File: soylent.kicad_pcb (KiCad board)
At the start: 2 copper layers, 23 parts, among them J1 DB9_Female, J2 Conn_01x04, J3 Conn_01x04, J4 Conn_02x03_Counter_Clockwise, Q1 BC847BPN, Q2 BC847BPN, U1 ATtiny202-SS, U2 MIC5504-3.3YM5

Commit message: Drop a via
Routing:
- net VDD: track 44.2 -> 46.4 mm
- net GND: vias 4 -> 3
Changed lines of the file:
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@@
   (segment (start 228.0258 37.3126) (end 226.1108 39.2276) (width 0.25) (layer B.Cu) (net 1))
   (segment (start 234.5944 37.3126) (end 228.0258 37.3126) (width 0.25) (layer B.Cu) (net 1))
-  (via (at 241.6048 32.3826) (size 0.8) (drill 0.4) (layers F.Cu B.Cu) (net 1))
   (via (at 237.3884 29.9212) (size 0.8) (drill 0.4) (layers F.Cu B.Cu) (net 1))
   (segment (start 232.961611 56.076011) (end 225.0058 48.1202) (width 0.25) (layer F.Cu) (net 2))
@@
   (segment (start 248.3642 31.2626) (end 248.5992 31.0276) (width 0.25) (layer F.Cu) (net 3))
   (segment (start 239.8672 31.2626) (end 248.3642 31.2626) (width 0.25) (layer F.Cu) (net 3))
-  (segment (start 248.5992 32.655) (end 248.5992 31.0276) (width 0.25) (layer F.Cu) (net 3))
-  (segment (start 243.9416 37.3126) (end 248.5992 32.655) (width 0.25) (layer F.Cu) (net 3))
+  (segment (start 251.2236 39.2076) (end 252.3236 39.2076) (width 0.25) (layer F.Cu) (net 3))
+  (segment (start 248.5992 36.5832) (end 251.2236 39.2076) (width 0.25) (layer F.Cu) (net 3))
+  (segment (start 248.5992 31.0276) (end 248.5992 36.5832) (width 0.25) (layer F.Cu) (net 3))
   (segment (start 227.2058 49.539602) (end 227.2058 45.212) (width 0.25) (layer F.Cu) (net 4))
   (segment (start 235.798601 55.620988) (end 234.345799 55.620988) (width 0.25) (layer F.Cu) (net 4))

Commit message: Add edge cuts
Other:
- board outline added: 34.5 x 44.2 mm
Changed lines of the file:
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@@
   (general
     (thickness 1.6)
-    (drawings 2)
+    (drawings 6)
     (tracks 160)
     (zones 0)
@@
     )
   )
+  (gr_line (start 221.8944 64.008) (end 221.8944 19.7612) (layer Edge.Cuts) (width 0.1))
+  (gr_line (start 256.3876 64.008) (end 221.8944 64.008) (layer Edge.Cuts) (width 0.1))
+  (gr_line (start 256.3876 19.7612) (end 256.3876 64.008) (layer Edge.Cuts) (width 0.1))
+  (gr_line (start 221.8944 19.7612) (end 256.3876 19.7612) (layer Edge.Cuts) (width 0.1))
   (gr_text Vdd (at 254.6096 39.1668 90) (layer F.SilkS)
     (effects (font (size 1 1) (thickness 0.25)))

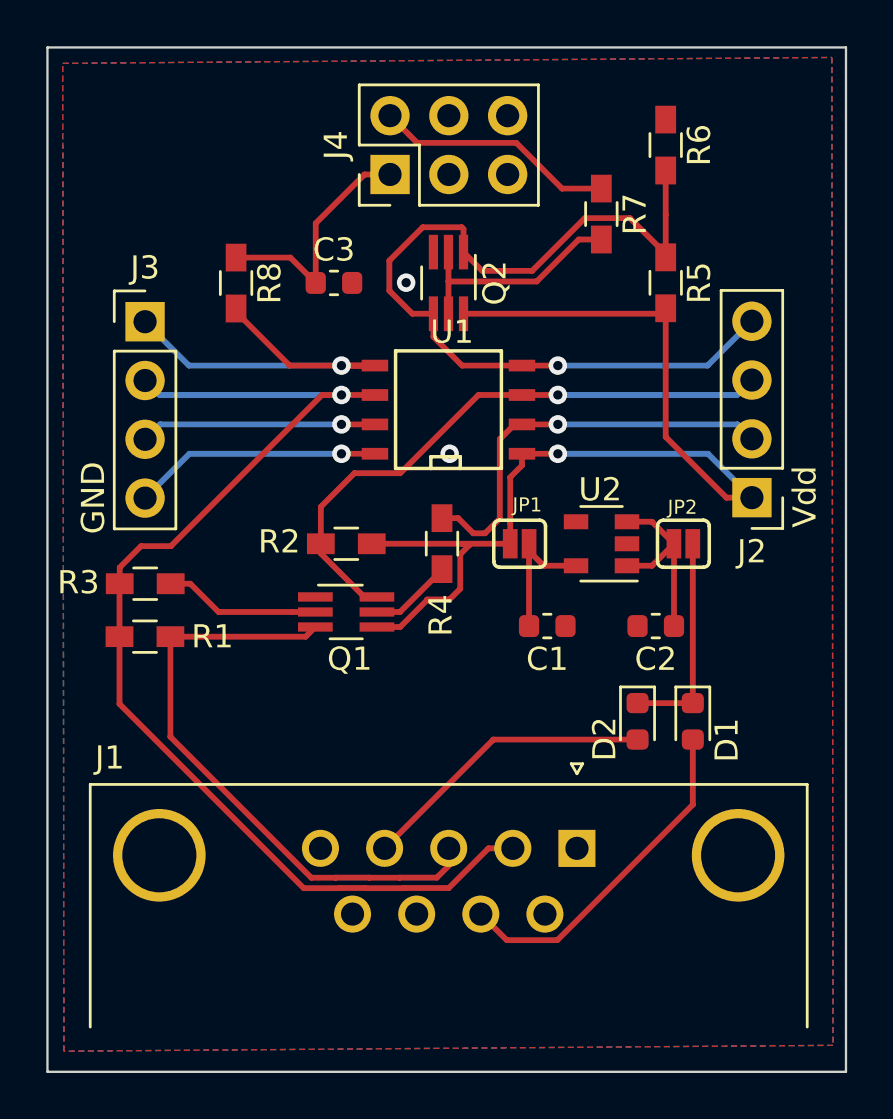
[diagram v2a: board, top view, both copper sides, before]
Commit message: Shrink cuts and zones
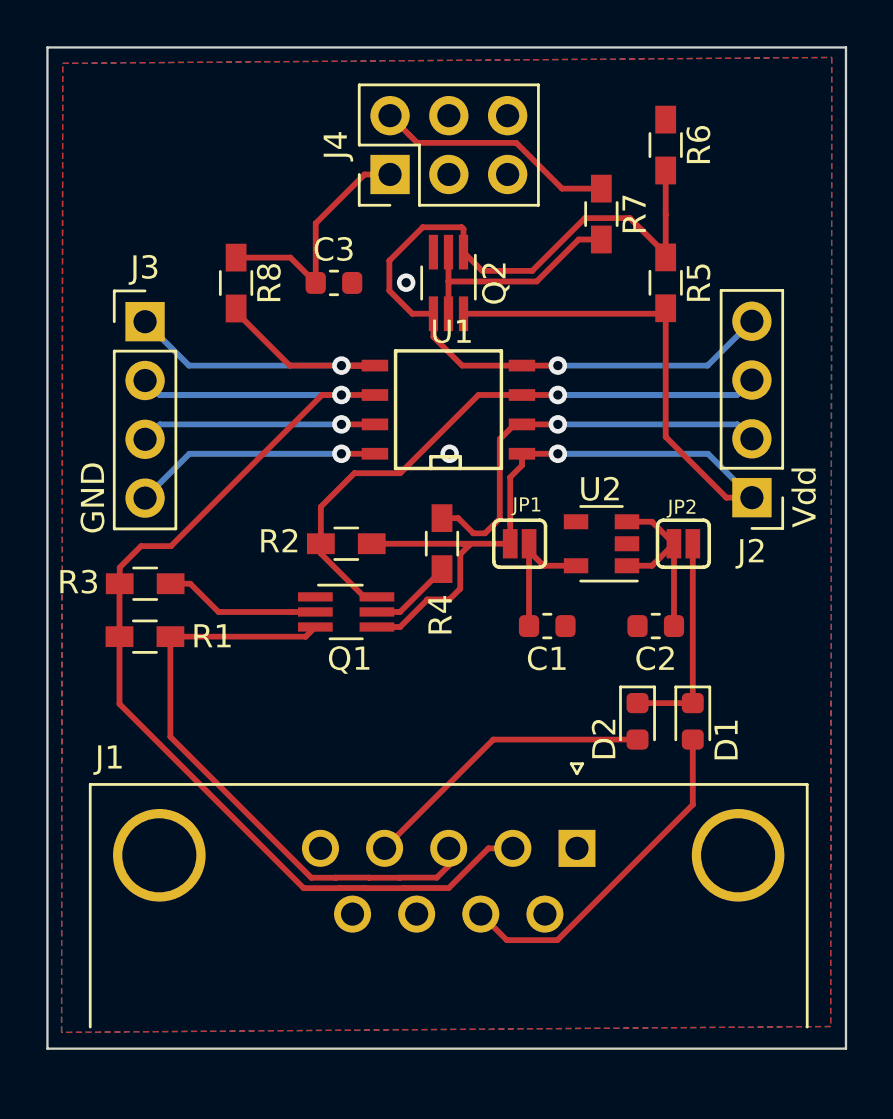
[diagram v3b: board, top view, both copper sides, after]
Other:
- board size 34.5 x 44.2 mm -> 34.5 x 43.2 mm
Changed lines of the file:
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@@
     )
   )
-  (gr_line (start 221.8944 64.008) (end 221.8944 19.7612) (layer Edge.Cuts) (width 0.1))
-  (gr_line (start 256.3876 64.008) (end 221.8944 64.008) (layer Edge.Cuts) (width 0.1))
-  (gr_line (start 256.3876 19.7612) (end 256.3876 64.008) (layer Edge.Cuts) (width 0.1))
+  (gr_line (start 221.8944 63.008) (end 221.8944 19.7612) (layer Edge.Cuts) (width 0.1))
+  (gr_line (start 256.3876 63.008) (end 221.8944 63.008) (layer Edge.Cuts) (width 0.1))
+  (gr_line (start 256.3876 19.7612) (end 256.3876 63.008) (layer Edge.Cuts) (width 0.1))
   (gr_line (start 221.8944 19.7612) (end 256.3876 19.7612) (layer Edge.Cuts) (width 0.1))
   (gr_text Vdd (at 254.6096 39.1668 90) (layer F.SilkS)
@@
     (polygon
       (pts
-        (xy 222.5548 20.447) (xy 255.778 20.193) (xy 255.8288 62.865) (xy 222.6056 63.119)
+        (xy 222.5548 20.447) (xy 255.778 20.193) (xy 255.7272 62.0522) (xy 222.504 62.3062)
       )
     )
@@
     (polygon
       (pts
-        (xy 222.5548 20.447) (xy 255.778 20.193) (xy 255.8288 62.865) (xy 222.6056 63.119)
+        (xy 222.5548 20.447) (xy 255.778 20.193) (xy 255.7272 62.0522) (xy 222.504 62.3062)
       )
     )

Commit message: Routing tweaks
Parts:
- moved C3 6.92 mm to (230.0, 24.5), turned to 90 degrees
- moved R6 0.17 mm to (248.6, 24.1)
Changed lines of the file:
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@@
     (thickness 1.6)
     (drawings 6)
-    (tracks 160)
+    (tracks 158)
     (zones 0)
     (modules 23)
@@
   )
   (module Capacitor_SMD:C_0603_1608Metric (layer F.Cu)
-    (at 234.2708 29.9326)
+    (at 230.0422 24.4601 90)
     (descr "Capacitor SMD 0603 (1608 Metric), square (rectangular) end terminal, IPC_7351 nominal, (Body size source: http://www.tortai-tech.com/upload/download/2011102023233369053.pdf), generated with kicad-footprint-generator")
     (tags capacitor)
     (attr smd)
-    (fp_text reference C3 (at 0 -1.43) (layer F.SilkS)
-      (effects (font (size 1 1) (thickness 0.15)))
-    )
-    (fp_text value .1u (at 0 1.43) (layer F.Fab)
-      (effects (font (size 1 1) (thickness 0.15)))
-    )
-    (fp_text user %R (at 0 0) (layer F.Fab)
+    (fp_text reference C3 (at 0 -1.43 90) (layer F.SilkS)
+      (effects (font (size 1 1) (thickness 0.15)))
+    )
+    (fp_text value .1u (at 0 1.43 90) (layer F.Fab)
+      (effects (font (size 1 1) (thickness 0.15)))
+    )
+    (fp_text user %R (at 0 0 90) (layer F.Fab)
       (effects (font (size 0.4 0.4) (thickness 0.06)))
     )
@@
     (fp_line (start -0.8 -0.4) (end 0.8 -0.4) (layer F.Fab) (width 0.1))
     (fp_line (start -0.8 0.4) (end -0.8 -0.4) (layer F.Fab) (width 0.1))
-    (pad 2 smd roundrect (at 0.7875 0) (size 0.875 0.95) (layers F.Cu F.Paste F.Mask) (roundrect_rratio 0.25)
+    (pad 2 smd roundrect (at 0.7875 0 90) (size 0.875 0.95) (layers F.Cu F.Paste F.Mask) (roundrect_rratio 0.25)
       (net 1 GND))
-    (pad 1 smd roundrect (at -0.7875 0) (size 0.875 0.95) (layers F.Cu F.Paste F.Mask) (roundrect_rratio 0.25)
+    (pad 1 smd roundrect (at -0.7875 0 90) (size 0.875 0.95) (layers F.Cu F.Paste F.Mask) (roundrect_rratio 0.25)
       (net 19 "Net-(C3-Pad1)"))
     (model ${KISYS3DMOD}/Capacitor_SMD.3dshapes/C_0603_1608Metric.wrl
@@
   )
   (module Resistors_SMD:R_0603_HandSoldering (layer F.Cu)
-    (at 248.5992 23.9776 270)
+    (at 248.5992 24.1476 270)
     (descr "Resistor SMD 0603, hand soldering")
     (tags "resistor 0603")
@@
     (tags "resistor 0603")
     (attr smd)
-    (fp_text reference R3 (at -2.884 -0.0508) (layer F.SilkS)
-      (effects (font (size 1 1) (thickness 0.15)))
-    )
-    (fp_text value 10k (at 3.3136 0) (layer F.Fab)
+    (fp_text reference R3 (at 3.043 0) (layer F.SilkS)
+      (effects (font (size 1 1) (thickness 0.15)))
+    )
+    (fp_text value 10k (at 0.0458 1.016) (layer F.Fab)
       (effects (font (size 1 1) (thickness 0.15)))
     )
@@
       (effects (font (size 1 1) (thickness 0.15)))
     )
-    (fp_text value 4k7 (at 3.382 0.0508) (layer F.Fab)
+    (fp_text value 4k7 (at 0.0458 -1.524) (layer F.Fab)
       (effects (font (size 1 1) (thickness 0.15)))
     )
@@
     )
   )
-  (module Pin_Headers:Pin_Header_Straight_2x03_Pitch2.54mm locked (layer F.Cu)
+  (module Pin_Headers:Pin_Header_Straight_2x03_Pitch2.54mm (layer F.Cu)
     (at 236.6922 25.2476 90)
     (descr "Through hole straight pin header, 2x03, 2.54mm pitch, double rows")
@@
   (segment (start 226.7558 36.0426) (end 226.1108 36.6876) (width 0.25) (layer B.Cu) (net 17))
   (segment (start 234.5944 36.0426) (end 226.7558 36.0426) (width 0.25) (layer B.Cu) (net 17))
-  (segment (start 248.5992 26.9908) (end 248.5992 28.8276) (width 0.25) (layer F.Cu) (net 15))
-  (segment (start 248.5992 25.0776) (end 248.5992 26.9908) (width 0.25) (layer F.Cu) (net 15))
-  (segment (start 245.111199 27.132599) (end 247.054199 27.132599) (width 0.25) (layer F.Cu) (net 15))
-  (segment (start 242.830598 29.4132) (end 245.111199 27.132599) (width 0.25) (layer F.Cu) (net 15))
-  (segment (start 248.5992 28.6776) (end 248.5992 28.8276) (width 0.25) (layer F.Cu) (net 15))
-  (segment (start 240.6778 29.4132) (end 242.830598 29.4132) (width 0.25) (layer F.Cu) (net 15))
-  (segment (start 247.054199 27.132599) (end 248.5992 28.6776) (width 0.25) (layer F.Cu) (net 15))
-  (segment (start 239.8672 28.6026) (end 240.6778 29.4132) (width 0.25) (layer F.Cu) (net 15))
   (segment (start 238.5672 32.2626) (end 238.5672 31.2626) (width 0.25) (layer F.Cu) (net 15))
   (segment (start 239.8072 33.5026) (end 238.5672 32.2626) (width 0.25) (layer F.Cu) (net 15))
@@
   (segment (start 239.792199 27.527599) (end 239.8672 27.6026) (width 0.25) (layer F.Cu) (net 15))
   (segment (start 238.5672 31.2626) (end 237.656798 31.2626) (width 0.25) (layer F.Cu) (net 15))
+  (segment (start 248.5992 28.8276) (end 248.5992 28.6776) (width 0.25) (layer F.Cu) (net 15))
+  (segment (start 248.5992 28.8276) (end 248.5992 25.2476) (width 0.25) (layer F.Cu) (net 15))
+  (segment (start 248.5992 25.3976) (end 248.5992 25.2476) (width 0.25) (layer F.Cu) (net 15))
+  (segment (start 239.8672 28.6026) (end 240.6778 29.4132) (width 0.25) (layer F.Cu) (net 15))
+  (segment (start 242.830598 29.4132) (end 245.268998 26.9748) (width 0.25) (layer F.Cu) (net 15))
+  (segment (start 240.6778 29.4132) (end 242.830598 29.4132) (width 0.25) (layer F.Cu) (net 15))
+  (segment (start 247.022 26.9748) (end 248.5992 25.3976) (width 0.25) (layer F.Cu) (net 15))
+  (segment (start 245.268998 26.9748) (end 247.022 26.9748) (width 0.25) (layer F.Cu) (net 15))
   (segment (start 230.0422 31.1876) (end 230.0422 31.0376) (width 0.25) (layer F.Cu) (net 16))
   (segment (start 232.3572 33.5026) (end 230.0422 31.1876) (width 0.25) (layer F.Cu) (net 16))
@@
   (segment (start 244.84 28.0576) (end 243.0272 29.8704) (width 0.25) (layer F.Cu) (net 18))
   (segment (start 245.8212 28.0576) (end 244.84 28.0576) (width 0.25) (layer F.Cu) (net 18))
-  (segment (start 235.5922 25.2476) (end 236.6922 25.2476) (width 0.25) (layer F.Cu) (net 19))
-  (segment (start 233.4833 27.3565) (end 235.5922 25.2476) (width 0.25) (layer F.Cu) (net 19))
-  (segment (start 233.4833 29.9326) (end 233.4833 27.3565) (width 0.25) (layer F.Cu) (net 19))
-  (segment (start 232.3883 28.8376) (end 233.4833 29.9326) (width 0.25) (layer F.Cu) (net 19))
-  (segment (start 230.0422 28.8376) (end 232.3883 28.8376) (width 0.25) (layer F.Cu) (net 19))
+  (segment (start 230.0422 25.2476) (end 236.6922 25.2476) (width 0.25) (layer F.Cu) (net 19))
+  (segment (start 230.0422 25.7851) (end 230.0422 28.8376) (width 0.25) (layer F.Cu) (net 19))
+  (segment (start 230.0422 25.2476) (end 230.0422 25.7851) (width 0.25) (layer F.Cu) (net 19))
   (zone (net 1) (net_name GND) (layer F.Cu) (hatch edge 0.508)
     (connect_pads (clearance 0.254))

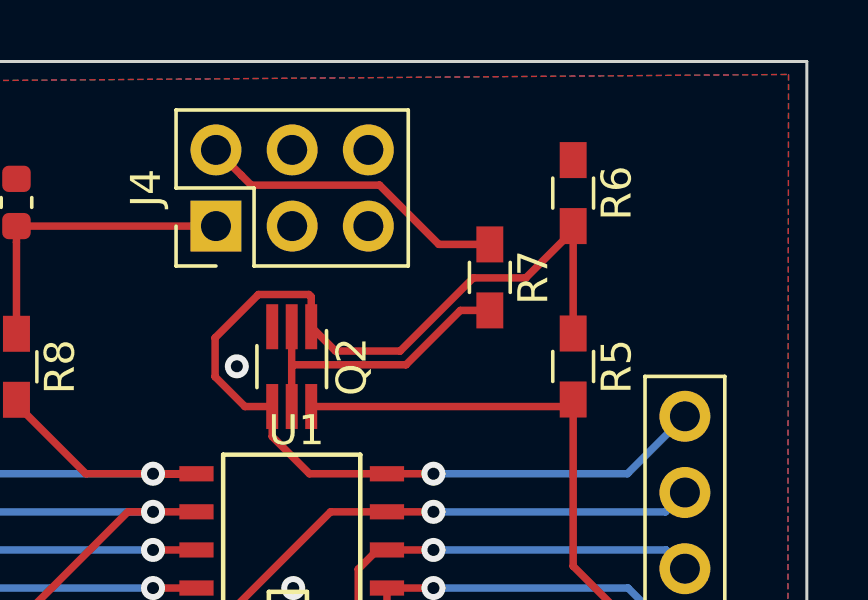
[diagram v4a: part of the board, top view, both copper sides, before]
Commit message: Rerouting with one fewer vias
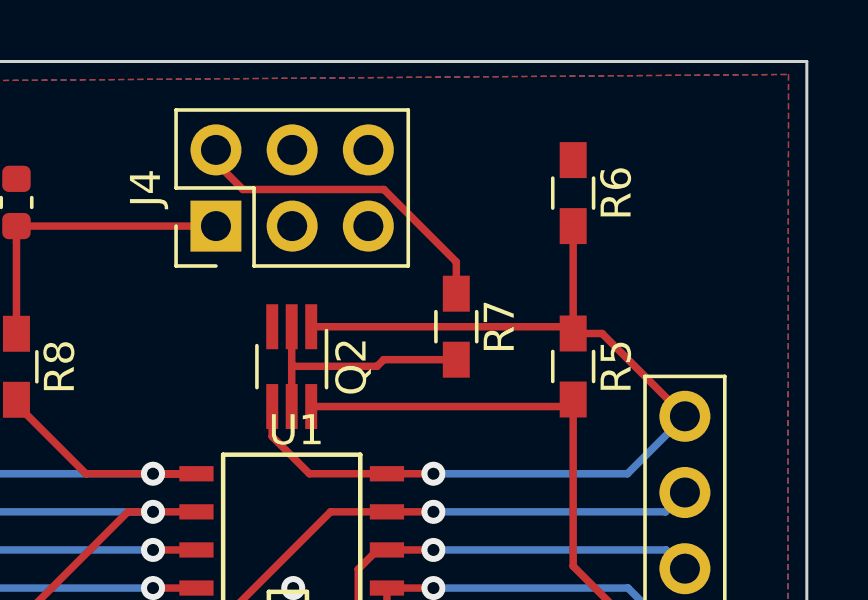
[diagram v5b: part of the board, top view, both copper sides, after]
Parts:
- moved R7 1.99 mm to (244.7, 28.6)
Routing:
- net /PA1: track 39.1 -> 33.5 mm
- net Net-(Q2-Pad2): track 10.0 -> 8.24 mm
- net GND: vias 3 -> 2
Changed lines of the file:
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@@
     (thickness 1.6)
     (drawings 6)
-    (tracks 158)
+    (tracks 148)
     (zones 0)
     (modules 23)
@@
   )
   (module Resistors_SMD:R_0603_HandSoldering (layer F.Cu)
-    (at 245.8212 26.9576 270)
+    (at 244.7036 28.6004 270)
     (descr "Resistor SMD 0603, hand soldering")
     (tags "resistor 0603")
@@
   (segment (start 228.0258 37.3126) (end 226.1108 39.2276) (width 0.25) (layer B.Cu) (net 1))
   (segment (start 234.5944 37.3126) (end 228.0258 37.3126) (width 0.25) (layer B.Cu) (net 1))
-  (via (at 237.3884 29.9212) (size 0.8) (drill 0.4) (layers F.Cu B.Cu) (net 1))
   (segment (start 232.961611 56.076011) (end 225.0058 48.1202) (width 0.25) (layer F.Cu) (net 2))
   (segment (start 225.0058 48.1202) (end 225.0058 45.212) (width 0.25) (layer F.Cu) (net 2))
@@
   (segment (start 249.7708 52.472402) (end 249.7708 49.6571) (width 0.25) (layer F.Cu) (net 10))
   (segment (start 240.6122 57.196) (end 241.737201 58.321001) (width 0.25) (layer F.Cu) (net 10))
-  (segment (start 237.542199 23.557599) (end 236.6922 22.7076) (width 0.25) (layer F.Cu) (net 11))
-  (segment (start 237.867201 23.882601) (end 237.542199 23.557599) (width 0.25) (layer F.Cu) (net 11))
-  (segment (start 242.146203 23.882601) (end 237.867201 23.882601) (width 0.25) (layer F.Cu) (net 11))
-  (segment (start 244.121202 25.8576) (end 242.146203 23.882601) (width 0.25) (layer F.Cu) (net 11))
-  (segment (start 245.8212 25.8576) (end 244.121202 25.8576) (width 0.25) (layer F.Cu) (net 11))
+  (segment (start 236.6922 23.129) (end 236.6922 22.7076) (width 0.25) (layer F.Cu) (net 11))
+  (segment (start 237.5916 24.0284) (end 236.6922 23.129) (width 0.25) (layer F.Cu) (net 11))
+  (segment (start 242.292002 24.0284) (end 237.5916 24.0284) (width 0.25) (layer F.Cu) (net 11))
+  (segment (start 244.7036 26.439998) (end 242.292002 24.0284) (width 0.25) (layer F.Cu) (net 11))
+  (segment (start 244.7036 27.5004) (end 244.7036 26.439998) (width 0.25) (layer F.Cu) (net 11))
   (segment (start 249.7708 41.1988) (end 249.7708 48.0821) (width 0.25) (layer F.Cu) (net 12))
   (segment (start 249.7708 48.0821) (end 247.383 48.0821) (width 0.25) (layer F.Cu) (net 12))
@@
   (segment (start 239.8072 33.5026) (end 238.5672 32.2626) (width 0.25) (layer F.Cu) (net 15))
   (segment (start 242.3922 33.5026) (end 239.8072 33.5026) (width 0.25) (layer F.Cu) (net 15))
-  (segment (start 239.8672 27.6026) (end 239.8672 28.6026) (width 0.25) (layer F.Cu) (net 15))
-  (segment (start 238.107199 27.527599) (end 239.792199 27.527599) (width 0.25) (layer F.Cu) (net 15))
-  (segment (start 236.663399 28.971399) (end 238.107199 27.527599) (width 0.25) (layer F.Cu) (net 15))
-  (segment (start 236.663399 30.269201) (end 236.663399 28.971399) (width 0.25) (layer F.Cu) (net 15))
-  (segment (start 237.656798 31.2626) (end 236.663399 30.269201) (width 0.25) (layer F.Cu) (net 15))
-  (segment (start 239.792199 27.527599) (end 239.8672 27.6026) (width 0.25) (layer F.Cu) (net 15))
-  (segment (start 238.5672 31.2626) (end 237.656798 31.2626) (width 0.25) (layer F.Cu) (net 15))
   (segment (start 248.5992 28.8276) (end 248.5992 28.6776) (width 0.25) (layer F.Cu) (net 15))
   (segment (start 248.5992 28.8276) (end 248.5992 25.2476) (width 0.25) (layer F.Cu) (net 15))
-  (segment (start 248.5992 25.3976) (end 248.5992 25.2476) (width 0.25) (layer F.Cu) (net 15))
-  (segment (start 239.8672 28.6026) (end 240.6778 29.4132) (width 0.25) (layer F.Cu) (net 15))
-  (segment (start 242.830598 29.4132) (end 245.268998 26.9748) (width 0.25) (layer F.Cu) (net 15))
-  (segment (start 240.6778 29.4132) (end 242.830598 29.4132) (width 0.25) (layer F.Cu) (net 15))
-  (segment (start 247.022 26.9748) (end 248.5992 25.3976) (width 0.25) (layer F.Cu) (net 15))
-  (segment (start 245.268998 26.9748) (end 247.022 26.9748) (width 0.25) (layer F.Cu) (net 15))
+  (segment (start 248.3742 28.6026) (end 248.5992 28.8276) (width 0.25) (layer F.Cu) (net 15))
+  (segment (start 239.8672 28.6026) (end 248.3742 28.6026) (width 0.25) (layer F.Cu) (net 15))
+  (segment (start 249.5636 28.8276) (end 252.3236 31.5876) (width 0.25) (layer F.Cu) (net 15))
+  (segment (start 248.5992 28.8276) (end 249.5636 28.8276) (width 0.25) (layer F.Cu) (net 15))
   (segment (start 230.0422 31.1876) (end 230.0422 31.0376) (width 0.25) (layer F.Cu) (net 16))
   (segment (start 232.3572 33.5026) (end 230.0422 31.1876) (width 0.25) (layer F.Cu) (net 16))
   (segment (start 236.0422 33.5026) (end 232.3572 33.5026) (width 0.25) (layer F.Cu) (net 16))
-  (segment (start 239.2172 29.8704) (end 239.2172 28.6026) (width 0.25) (layer F.Cu) (net 18))
-  (segment (start 239.2172 31.2626) (end 239.2172 29.8704) (width 0.25) (layer F.Cu) (net 18))
-  (segment (start 243.0272 29.8704) (end 239.2172 29.8704) (width 0.25) (layer F.Cu) (net 18))
-  (segment (start 244.84 28.0576) (end 243.0272 29.8704) (width 0.25) (layer F.Cu) (net 18))
-  (segment (start 245.8212 28.0576) (end 244.84 28.0576) (width 0.25) (layer F.Cu) (net 18))
+  (segment (start 239.2172 29.9212) (end 239.2172 28.6026) (width 0.25) (layer F.Cu) (net 18))
+  (segment (start 239.2172 31.2626) (end 239.2172 29.9212) (width 0.25) (layer F.Cu) (net 18))
+  (segment (start 242.2828 29.7004) (end 244.7036 29.7004) (width 0.25) (layer F.Cu) (net 18))
+  (segment (start 242.062 29.9212) (end 242.2828 29.7004) (width 0.25) (layer F.Cu) (net 18))
+  (segment (start 239.2172 29.9212) (end 242.062 29.9212) (width 0.25) (layer F.Cu) (net 18))
   (segment (start 230.0422 25.2476) (end 236.6922 25.2476) (width 0.25) (layer F.Cu) (net 19))
   (segment (start 230.0422 25.7851) (end 230.0422 28.8376) (width 0.25) (layer F.Cu) (net 19))
